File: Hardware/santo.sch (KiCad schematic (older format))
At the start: 10 parts, among them J1 USB_C_Receptacle, J2 USB_C_Receptacle, U1 ATMEGA32U4-MU

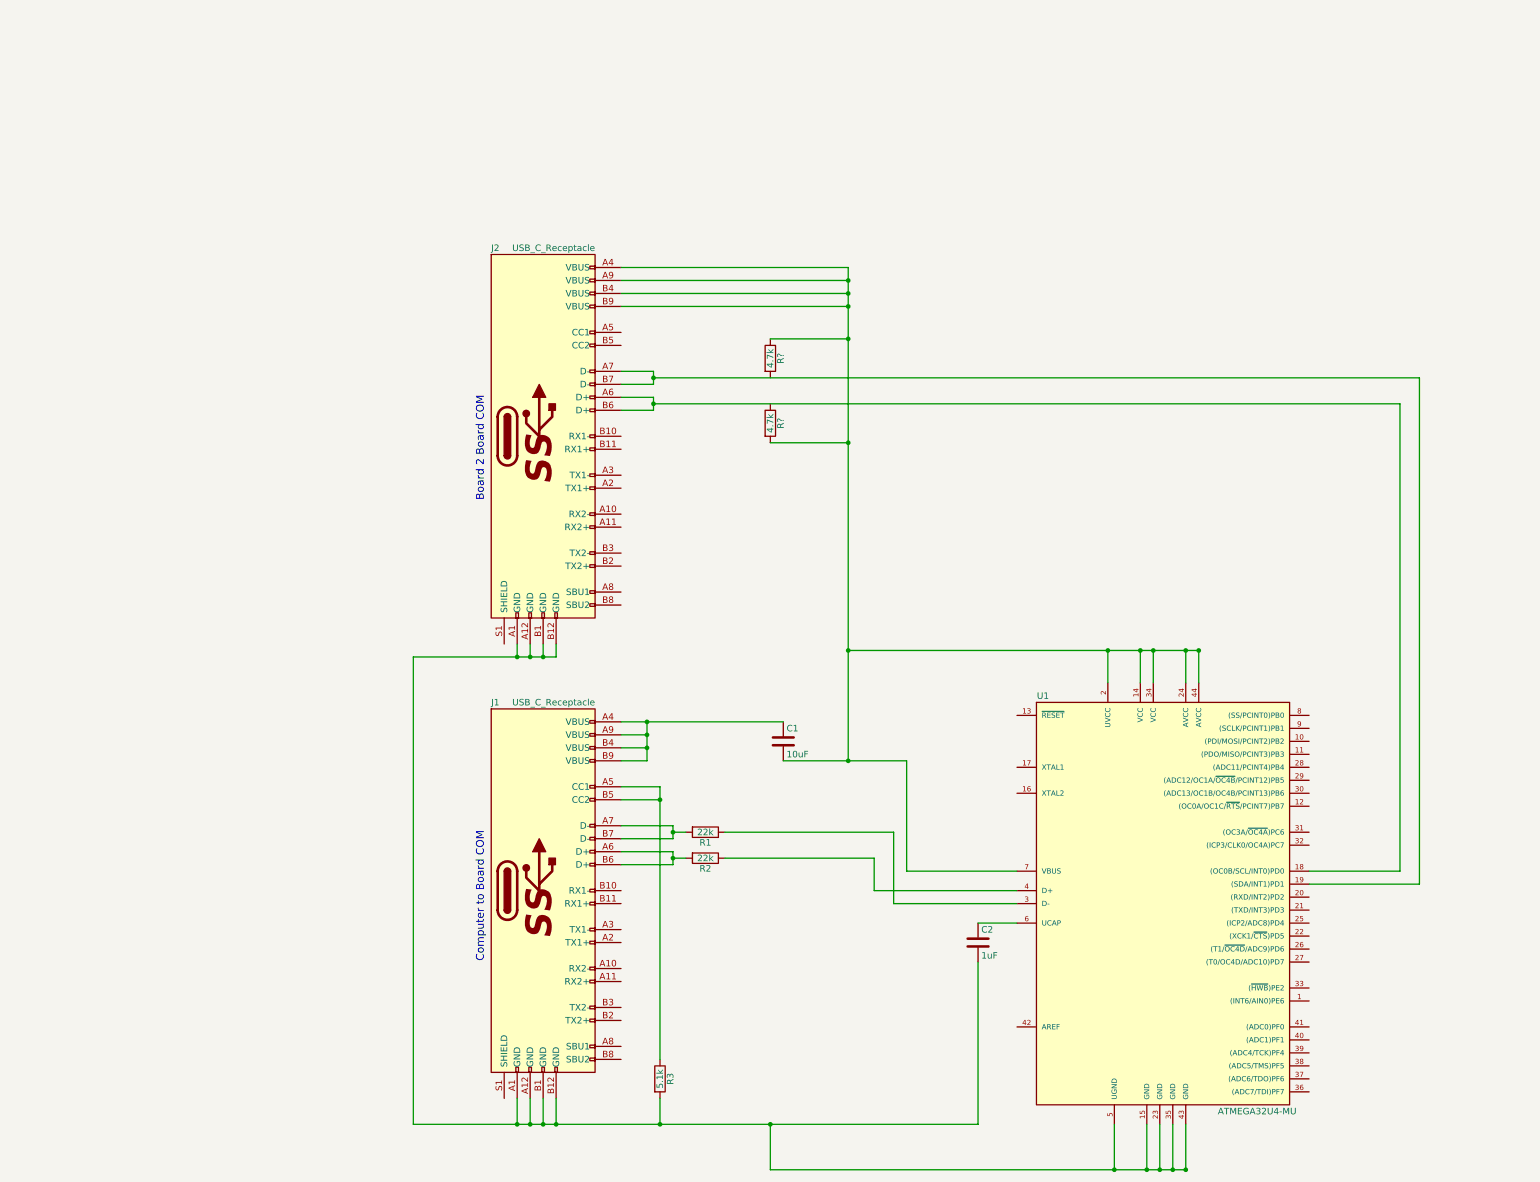
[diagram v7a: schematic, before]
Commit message: Change to BUS for the SCL/SDA.
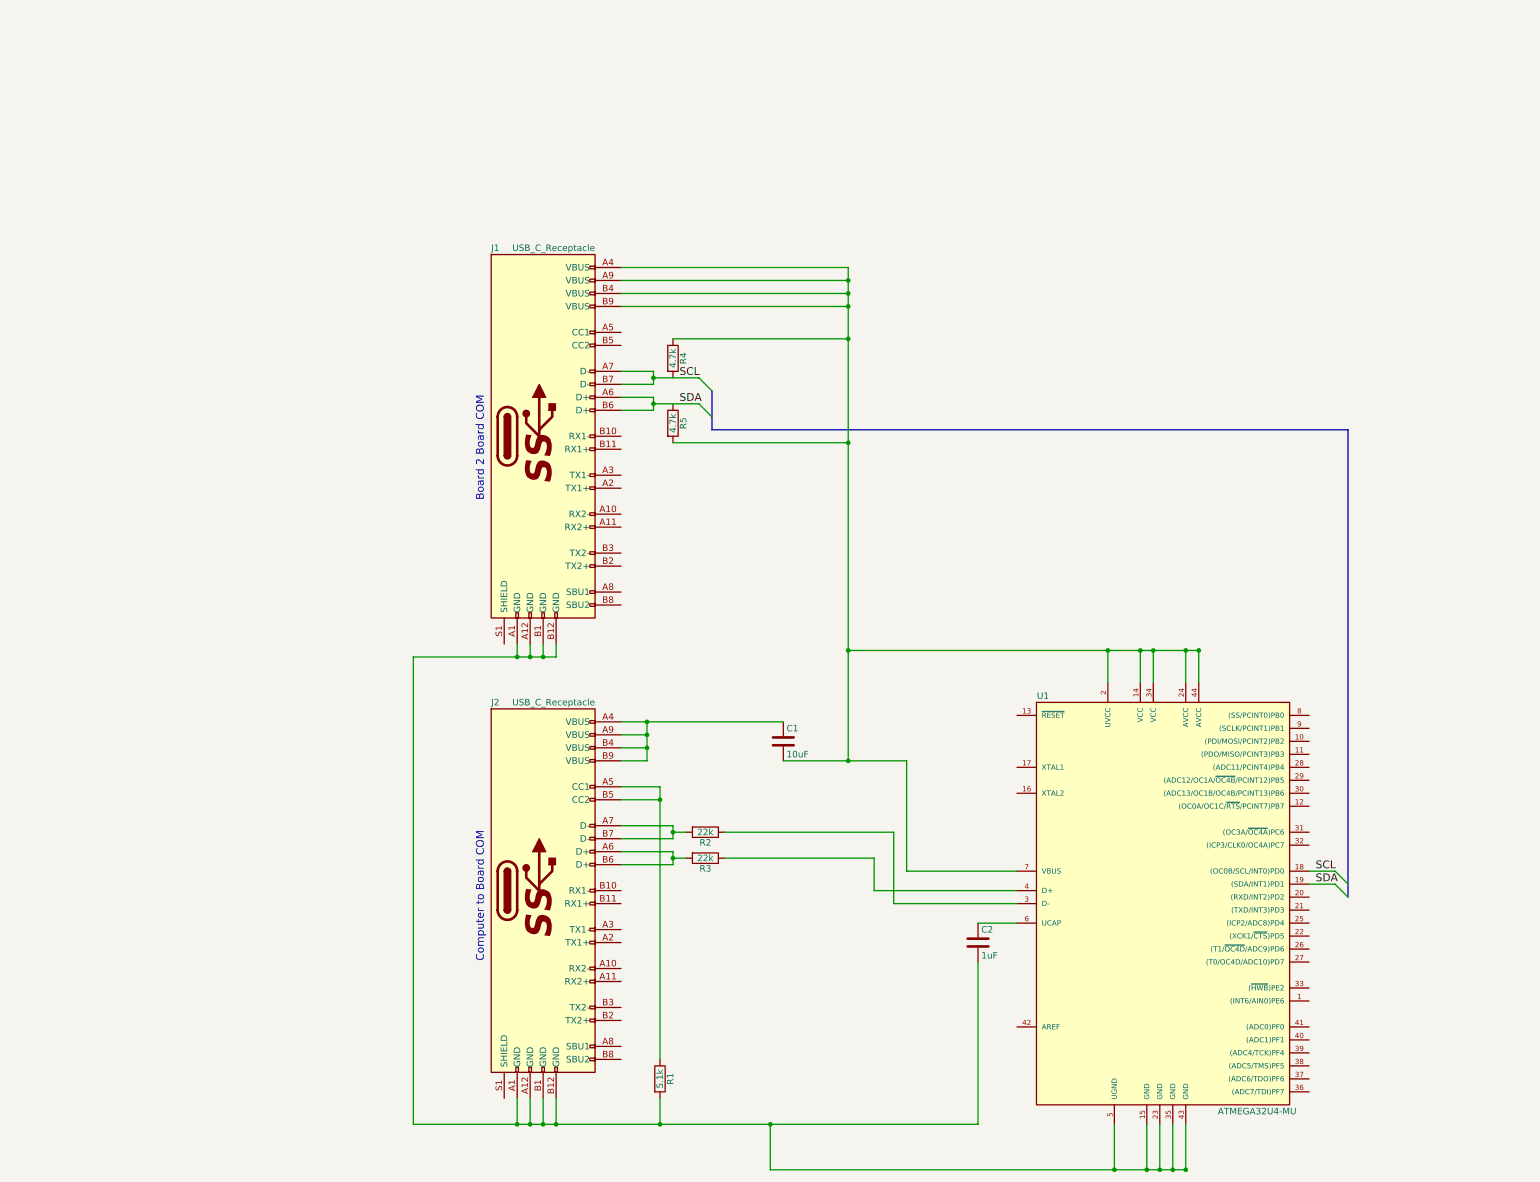
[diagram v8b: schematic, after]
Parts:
- gave numbers to parts that had none: 2
- renumbered J2 to J1, J1 to J2, R3 to R1, R1 to R2, R2 to R3
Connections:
- net SDA: now reaches J1.A6 (D+), J1.B6 (D+)
- net SDA: now also U1.19 ((SDA/INT1)PD1); no longer U1.18 ((OC0B/SCL/INT0)PD0)
- net SCL: now reaches J1.A7 (D-), J1.B7 (D-)
- net SCL: now also U1.18 ((OC0B/SCL/INT0)PD0); no longer U1.19 ((SDA/INT1)PD1)
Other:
- moved on the sheet: R4, R5
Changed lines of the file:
@@
 $EndDescr
 $Comp
-L USB_C_Receptacle J1
+L USB_C_Receptacle J2
 U 1 1 59F5288B
 P 4700 8300
-F 0 "J1" H 4300 9750 50  0000 L CNN
+F 0 "J2" H 4300 9750 50  0000 L CNN
 F 1 "USB_C_Receptacle" H 5100 9750 50  0000 R CNN
 F 2 "" H 4850 8300 50  0001 C CNN
@@
 $EndComp
 $Comp
-L R R3
+L R R1
 U 1 1 59F605C4
 P 5600 9750
-F 0 "R3" V 5680 9750 50  0000 C CNN
+F 0 "R1" V 5680 9750 50  0000 C CNN
 F 1 "5.1k" V 5600 9750 50  0000 C CNN
 F 2 "" V 5530 9750 50  0001 C CNN
@@
 $EndComp
 $Comp
-L R R1
+L R R2
 U 1 1 59F60892
 P 5950 7850
-F 0 "R1" V 6030 7850 50  0000 C CNN
+F 0 "R2" V 6030 7850 50  0000 C CNN
 F 1 "22k" V 5950 7850 50  0000 C CNN
 F 2 "" V 5880 7850 50  0001 C CNN
@@
 $EndComp
 $Comp
-L R R2
+L R R3
 U 1 1 59F608F2
 P 5950 8050
-F 0 "R2" V 6030 8050 50  0000 C CNN
+F 0 "R3" V 6030 8050 50  0000 C CNN
 F 1 "22k" V 5950 8050 50  0000 C CNN
 F 2 "" V 5880 8050 50  0001 C CNN
@@
 $EndComp
 $Comp
-L USB_C_Receptacle J2
+L USB_C_Receptacle J1
 U 1 1 5A08C066
 P 4700 4800
-F 0 "J2" H 4300 6250 50  0000 L CNN
+F 0 "J1" H 4300 6250 50  0000 L CNN
 F 1 "USB_C_Receptacle" H 5100 6250 50  0000 R CNN
 F 2 "" H 4850 4800 50  0001 C CNN
@@
 $EndComp
 $Comp
-L R R?
+L R R5
 U 1 1 5A08D231
-P 6450 4700
-F 0 "R?" V 6530 4700 50  0000 C CNN
-F 1 "4.7k" V 6450 4700 50  0000 C CNN
-F 2 "" V 6380 4700 50  0001 C CNN
-F 3 "" H 6450 4700 50  0001 C CNN
-	1    6450 4700
-	1    0    0    -1
-$EndComp
-$Comp
-L R R?
+P 5700 4700
+F 0 "R5" V 5780 4700 50  0000 C CNN
+F 1 "4.7k" V 5700 4700 50  0000 C CNN
+F 2 "" V 5630 4700 50  0001 C CNN
+F 3 "" H 5700 4700 50  0001 C CNN
+	1    5700 4700
+	1    0    0    -1
+$EndComp
+$Comp
+L R R4
 U 1 1 5A08D288
-P 6450 4200
-F 0 "R?" V 6530 4200 50  0000 C CNN
-F 1 "4.7k" V 6450 4200 50  0000 C CNN
-F 2 "" V 6380 4200 50  0001 C CNN
-F 3 "" H 6450 4200 50  0001 C CNN
-	1    6450 4200
-	1    0    0    -1
-$EndComp
-Wire Wire Line
-	6550 7300 7500 7300
-Connection ~ 7050 7300
-Connection ~ 9050 6450
-Wire Wire Line
-	7050 3500 7050 7300
-Wire Wire Line
-	10600 8250 11450 8250
-Wire Wire Line
-	10600 8150 11300 8150
-Wire Wire Line
-	7250 8300 8350 8300
-Wire Wire Line
-	7250 8050 7250 8300
-Wire Wire Line
-	6100 8050 7250 8050
-Wire Wire Line
-	7400 8400 8350 8400
-Wire Wire Line
-	7400 7850 7400 8400
-Wire Wire Line
-	6100 7850 7400 7850
-Connection ~ 5700 8050
-Wire Wire Line
-	5300 8000 5700 8000
-Wire Wire Line
-	5700 8050 5800 8050
-Wire Wire Line
-	5700 8000 5700 8100
-Wire Wire Line
-	5700 8100 5300 8100
-Connection ~ 5700 7850
-Wire Wire Line
-	5700 7900 5300 7900
-Wire Wire Line
-	5700 7850 5800 7850
-Wire Wire Line
-	5700 7800 5700 7900
-Wire Wire Line
-	5300 7800 5700 7800
-Connection ~ 5600 10100
-Wire Wire Line
-	5600 9900 5600 10100
-Connection ~ 5600 7600
-Wire Wire Line
-	5300 7600 5600 7600
-Wire Wire Line
-	5600 7500 5600 9600
-Wire Wire Line
-	5300 7500 5600 7500
-Connection ~ 9650 10450
-Wire Wire Line
-	9650 10100 9650 10450
-Connection ~ 9550 10450
-Wire Wire Line
-	9550 10100 9550 10450
-Connection ~ 9450 10450
-Wire Wire Line
-	9450 10100 9450 10450
-Connection ~ 9350 10450
-Wire Wire Line
-	9350 10100 9350 10450
-Connection ~ 9750 6450
-Wire Wire Line
-	9750 6450 9750 6700
-Connection ~ 9650 6450
-Wire Wire Line
-	9650 6450 9650 6700
-Connection ~ 9400 6450
-Wire Wire Line
-	9400 6450 9400 6700
-Connection ~ 9300 6450
-Wire Wire Line
-	9300 6450 9300 6700
-Connection ~ 6450 10100
-Wire Wire Line
-	6450 10450 6450 10100
-Wire Wire Line
-	9050 6700 9050 6450
-Connection ~ 4800 10100
-Wire Wire Line
-	4800 9900 4800 10100
-Connection ~ 4700 10100
-Wire Wire Line
-	4700 9900 4700 10100
-Connection ~ 4600 10100
-Wire Wire Line
-	4600 9900 4600 10100
-Wire Wire Line
-	4500 10100 4500 9900
-Wire Wire Line
-	3700 10100 8050 10100
-Wire Wire Line
-	8050 10100 8050 8850
-Wire Wire Line
-	8050 8550 8350 8550
-Wire Wire Line
-	7500 8150 8350 8150
-Wire Wire Line
-	7500 7300 7500 8150
-Wire Wire Line
-	5300 7000 6550 7000
-Connection ~ 5500 7200
-Wire Wire Line
-	5500 7300 5300 7300
-Connection ~ 5500 7100
-Wire Wire Line
-	5500 7200 5300 7200
-Connection ~ 5500 7000
-Wire Wire Line
-	5500 7000 5500 7300
-Wire Wire Line
-	5300 7100 5500 7100
-Connection ~ 7050 6450
-Wire Wire Line
-	9100 10100 9100 10450
-Connection ~ 9100 10450
-Wire Wire Line
-	7050 6450 9750 6450
-Wire Wire Line
-	9650 10450 6450 10450
-Wire Wire Line
-	7050 3500 5300 3500
-Wire Wire Line
-	5300 3600 7050 3600
-Connection ~ 7050 3600
-Wire Wire Line
-	5300 3700 7050 3700
-Connection ~ 7050 3700
-Wire Wire Line
-	5300 3800 7050 3800
-Connection ~ 7050 3800
-Wire Wire Line
-	11300 8150 11300 4550
-Wire Wire Line
-	11300 4550 5550 4550
-Wire Wire Line
-	5550 4500 5550 4600
-Wire Wire Line
-	5550 4500 5300 4500
-Wire Wire Line
-	5550 4600 5300 4600
-Connection ~ 5550 4550
-Wire Wire Line
-	11450 8250 11450 4350
-Wire Wire Line
-	11450 4350 5550 4350
-Wire Wire Line
-	5550 4300 5550 4400
-Wire Wire Line
-	5550 4300 5300 4300
-Wire Wire Line
-	5550 4400 5300 4400
-Connection ~ 5550 4350
-Wire Wire Line
-	6450 4050 7050 4050
-Connection ~ 7050 4050
-Wire Wire Line
-	6450 4850 7050 4850
-Connection ~ 7050 4850
-Wire Wire Line
-	4500 6400 4500 6500
-Wire Wire Line
-	3700 6500 4800 6500
-Wire Wire Line
-	3700 6500 3700 10100
-Connection ~ 4500 10100
-Wire Wire Line
-	4600 6500 4600 6400
-Connection ~ 4500 6500
-Wire Wire Line
-	4700 6500 4700 6400
-Connection ~ 4600 6500
-Wire Wire Line
-	4800 6500 4800 6400
-Connection ~ 4700 6500
+P 5700 4200
+F 0 "R4" V 5780 4200 50  0000 C CNN
+F 1 "4.7k" V 5700 4200 50  0000 C CNN
+F 2 "" V 5630 4200 50  0001 C CNN
+F 3 "" H 5700 4200 50  0001 C CNN
+	1    5700 4200
+	1    0    0    -1
+$EndComp
 Text Notes 4250 5300 1    60   ~ 0
 Board 2 Board COM
 Text Notes 4250 8850 1    60   ~ 0
 Computer to Board COM
+Entry Wire Line
+	10800 8150 10900 8250
+Entry Wire Line
+	10800 8250 10900 8350
+Wire Wire Line
+	6550 7300 7500 7300
+Connection ~ 7050 7300
+Connection ~ 9050 6450
+Wire Wire Line
+	7050 3500 7050 7300
+Wire Wire Line
+	7250 8300 8350 8300
+Wire Wire Line
+	7250 8050 7250 8300
+Wire Wire Line
+	6100 8050 7250 8050
+Wire Wire Line
+	7400 8400 8350 8400
+Wire Wire Line
+	7400 7850 7400 8400
+Wire Wire Line
+	6100 7850 7400 7850
+Connection ~ 5700 8050
+Wire Wire Line
+	5300 8000 5700 8000
+Wire Wire Line
+	5700 8050 5800 8050
+Wire Wire Line
+	5700 8000 5700 8100
+Wire Wire Line
+	5700 8100 5300 8100
+Connection ~ 5700 7850
+Wire Wire Line
+	5700 7900 5300 7900
+Wire Wire Line
+	5700 7850 5800 7850
+Wire Wire Line
+	5700 7800 5700 7900
+Wire Wire Line
+	5300 7800 5700 7800
+Connection ~ 5600 10100
+Wire Wire Line
+	5600 9900 5600 10100
+Connection ~ 5600 7600
+Wire Wire Line
+	5300 7600 5600 7600
+Wire Wire Line
+	5600 7500 5600 9600
+Wire Wire Line
+	5300 7500 5600 7500
+Connection ~ 9650 10450
+Wire Wire Line
+	9650 10100 9650 10450
+Connection ~ 9550 10450
+Wire Wire Line
+	9550 10100 9550 10450
+Connection ~ 9450 10450
+Wire Wire Line
+	9450 10100 9450 10450
+Connection ~ 9350 10450
+Wire Wire Line
+	9350 10100 9350 10450
+Connection ~ 9750 6450
+Wire Wire Line
+	9750 6450 9750 6700
+Connection ~ 9650 6450
+Wire Wire Line
+	9650 6450 9650 6700
+Connection ~ 9400 6450
+Wire Wire Line
+	9400 6450 9400 6700
+Connection ~ 9300 6450
+Wire Wire Line
+	9300 6450 9300 6700
+Connection ~ 6450 10100
+Wire Wire Line
+	6450 10450 6450 10100
+Wire Wire Line
+	9050 6700 9050 6450
+Connection ~ 4800 10100
+Wire Wire Line
+	4800 9900 4800 10100
+Connection ~ 4700 10100
+Wire Wire Line
+	4700 9900 4700 10100
+Connection ~ 4600 10100
+Wire Wire Line
+	4600 9900 4600 10100
+Wire Wire Line
+	4500 10100 4500 9900
+Wire Wire Line
+	3700 10100 8050 10100
+Wire Wire Line
+	8050 10100 8050 8850
+Wire Wire Line
+	8050 8550 8350 8550
+Wire Wire Line
+	7500 8150 8350 8150
+Wire Wire Line
+	7500 7300 7500 8150
+Wire Wire Line
+	5300 7000 6550 7000
+Connection ~ 5500 7200
+Wire Wire Line
+	5500 7300 5300 7300
+Connection ~ 5500 7100
+Wire Wire Line
+	5500 7200 5300 7200
+Connection ~ 5500 7000
+Wire Wire Line
+	5500 7000 5500 7300
+Wire Wire Line
+	5300 7100 5500 7100
+Connection ~ 7050 6450
+Wire Wire Line
+	9100 10100 9100 10450
+Connection ~ 9100 10450
+Wire Wire Line
+	7050 6450 9750 6450
+Wire Wire Line
+	9650 10450 6450 10450
+Wire Wire Line
+	7050 3500 5300 3500
+Wire Wire Line
+	5300 3600 7050 3600
+Connection ~ 7050 3600
+Wire Wire Line
+	5300 3700 7050 3700
+Connection ~ 7050 3700
+Wire Wire Line
+	5300 3800 7050 3800
+Connection ~ 7050 3800
+Wire Wire Line
+	5550 4500 5550 4600
+Wire Wire Line
+	5550 4500 5300 4500
+Wire Wire Line
+	5550 4600 5300 4600
+Connection ~ 5550 4550
+Wire Wire Line
+	5550 4300 5550 4400
+Wire Wire Line
+	5550 4300 5300 4300
+Wire Wire Line
+	5550 4400 5300 4400
+Connection ~ 5550 4350
+Wire Wire Line
+	5700 4050 7050 4050
+Connection ~ 7050 4050
+Wire Wire Line
+	5700 4850 7050 4850
+Connection ~ 7050 4850
+Wire Wire Line
+	4500 6400 4500 6500
+Wire Wire Line
+	3700 6500 4800 6500
+Wire Wire Line
+	3700 6500 3700 10100
+Connection ~ 4500 10100
+Wire Wire Line
+	4600 6500 4600 6400
+Connection ~ 4500 6500
+Wire Wire Line
+	4700 6500 4700 6400
+Connection ~ 4600 6500
+Wire Wire Line
+	4800 6500 4800 6400
+Connection ~ 4700 6500
+Wire Wire Line
+	10600 8150 10800 8150
+Wire Wire Line
+	10600 8250 10800 8250
+Wire Wire Line
+	5550 4350 5900 4350
+Wire Wire Line
+	5550 4550 5900 4550
+Entry Wire Line
+	5900 4350 6000 4450
+Entry Wire Line
+	5900 4550 6000 4650
+Wire Bus Line
+	10900 8350 10900 4750
+Wire Bus Line
+	10900 4750 6000 4750
+Wire Bus Line
+	6000 4750 6000 4450
+Text Label 5750 4550 0    60   ~ 0
+SDA
+Text Label 5750 4350 0    60   ~ 0
+SCL
+Text Label 10650 8150 0    60   ~ 0
+SCL
+Text Label 10650 8250 0    60   ~ 0
+SDA
 $EndSCHEMATC
